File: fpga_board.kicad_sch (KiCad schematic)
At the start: 157 parts, among them Q1 2N7002PW, Q2 2N7002PW, Q3 2N7002PW, Q4 2N7002PW, Q5 2N7002PW, Q6 2N7002PW, SW1 1TS028A-1300-0600-CT, U1 LFE5U-45F-7BG256I, U10 TLV62569DRL, U2 CYUSB3014-BZXC, U3 TLV62569DRL, U5 K4B4G1646E-BCMA, U6 K4B4G1646E-BCMA, U7 TLV62569DRL, U8 TLV62569DRL, U9 TLV62569DRL, X1 XO32, Y1 Crystal_GND24

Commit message: fpga active oscillator pin changed and layout fully constructed. B.Cu ACC lines slightly modified and FPGA fifo lanes slightly modified to free GPLL input pin
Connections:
- net 1v35: now also C57.1, R24.1, X1.4 (V+)
- net 3v3: no longer C57.1, R24.1, X1.4 (V+)
- net FIFO_DQ21: now also U1.B4 (PT11B); no longer U1.C5 (PT15A)
- net FIFO_DQ25: now also U1.D5 (PT13B); no longer U1.B3 (PT4B)
- net FIFO_DQ28: now also U1.C5 (PT15A); no longer U1.B4 (PT11B)
- net FIFO_DQ30: now also U1.B3 (PT4B); no longer U1.A2 (PT4A)
- net FPGA_CLK: now also U1.A2 (PT4A); no longer U1.T6 (PB4A)
- no-connect marks 75 -> 74
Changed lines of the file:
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@@
 	)
 	(no_connect
-		(at 370.84 557.53)
-	)
-	(no_connect
 		(at 148.59 542.29)
 	)
@@
 	)
 	(bus_entry
+		(at 387.35 557.53)
+		(size 2.54 -2.54)
+		(stroke
+			(width 0)
+			(type default)
+		)
+	)
+	(bus_entry
 		(at 386.08 458.47)
 		(size -2.54 2.54)
@@
 	)
 	(bus_entry
-		(at 389.89 544.83)
-		(size -2.54 2.54)
-		(stroke
-			(width 0)
-			(type default)
-		)
-	)
-	(bus_entry
 		(at 662.94 68.58)
 		(size 2.54 2.54)
@@
 	)
 	(bus_entry
-		(at 299.72 542.29)
-		(size 2.54 2.54)
-		(stroke
-			(width 0)
-			(type default)
-		)
-	)
-	(bus_entry
 		(at 125.73 501.65)
 		(size 2.54 2.54)
@@
 	)
 	(bus_entry
+		(at 387.35 547.37)
+		(size 2.54 -2.54)
+		(stroke
+			(width 0)
+			(type default)
+		)
+	)
+	(bus_entry
 		(at 353.06 218.44)
 		(size -2.54 2.54)
@@
 	(wire
 		(pts
-			(xy 302.26 544.83) (xy 325.12 544.83)
-		)
-		(stroke
-			(width 0)
-			(type default)
-		)
-	)
-	(wire
-		(pts
 			(xy 450.85 238.76) (xy 450.85 241.3)
 		)
@@
 	(wire
 		(pts
-			(xy 370.84 547.37) (xy 387.35 547.37)
-		)
-		(stroke
-			(width 0)
-			(type default)
-		)
-	)
-	(wire
-		(pts
 			(xy 784.86 114.3) (xy 774.7 114.3)
 		)
@@
 		)
 	)
+	(bus
+		(pts
+			(xy 389.89 544.83) (xy 389.89 547.37)
+		)
+		(stroke
+			(width 0)
+			(type default)
+		)
+	)
 	(wire
 		(pts
@@
 	(bus
 		(pts
-			(xy 389.89 539.75) (xy 389.89 544.83)
-		)
-		(stroke
-			(width 0)
-			(type default)
-		)
-	)
-	(bus
-		(pts
 			(xy 125.73 501.65) (xy 125.73 504.19)
 		)
@@
 	(bus
 		(pts
-			(xy 299.72 530.86) (xy 299.72 542.29)
+			(xy 299.72 530.86) (xy 299.72 544.83)
 		)
 		(stroke
@@
 	(bus
 		(pts
-			(xy 389.89 544.83) (xy 389.89 547.37)
+			(xy 389.89 539.75) (xy 389.89 544.83)
 		)
 		(stroke
@@
 	(wire
 		(pts
+			(xy 370.84 547.37) (xy 387.35 547.37)
+		)
+		(stroke
+			(width 0)
+			(type default)
+		)
+	)
+	(wire
+		(pts
 			(xy 547.37 237.49) (xy 549.91 237.49)
 		)
@@
 	(wire
 		(pts
+			(xy 370.84 557.53) (xy 387.35 557.53)
+		)
+		(stroke
+			(width 0)
+			(type default)
+		)
+	)
+	(wire
+		(pts
 			(xy 664.21 142.24) (xy 678.18 142.24)
 		)
@@
 		)
 	)
-	(bus
-		(pts
-			(xy 299.72 542.29) (xy 299.72 544.83)
-		)
-		(stroke
-			(width 0)
-			(type default)
-		)
-	)
 	(label "DM0"
 		(at 279.4 138.43 0)
@@
 		)
 	)
-	(label "FIFO_DQ28"
+	(label "FIFO_DQ21"
 		(at 370.84 549.91 0)
 		(effects
@@
 		)
 	)
-	(label "FIFO_DQ30"
-		(at 311.15 544.83 0)
+	(label "FIFO_DQ31"
+		(at 370.84 547.37 0)
 		(effects
 			(font
@@
 		)
 	)
-	(label "FIFO_DQ25"
+	(label "FIFO_DQ30"
 		(at 311.15 547.37 0)
 		(effects
@@
 		)
 	)
-	(label "FIFO_DQ21"
+	(label "FIFO_DQ28"
 		(at 571.5 463.55 0)
 		(effects
@@
 		)
 	)
-	(label "FIFO_DQ31"
-		(at 370.84 547.37 0)
+	(label "FIFO_DQ25"
+		(at 370.84 557.53 0)
 		(effects
 			(font
@@
 		)
 	)
-	(global_label "3v3"
+	(global_label "1v35"
 		(shape input)
 		(at 170.18 384.81 180)
@@
 		)
 		(property "Intersheetrefs" "${INTERSHEET_REFS}"
-			(at 163.8082 384.81 0)
+			(at 162.5987 384.81 0)
 			(effects
 				(font
@@
 	(global_label "FPGA_CLK"
 		(shape input)
-		(at 148.59 466.09 180)
+		(at 325.12 544.83 180)
 		(fields_autoplaced yes)
 		(effects
@@
 		)
 		(property "Intersheetrefs" "${INTERSHEET_REFS}"
-			(at 136.3519 466.09 0)
+			(at 312.8819 544.83 0)
 			(effects
 				(font

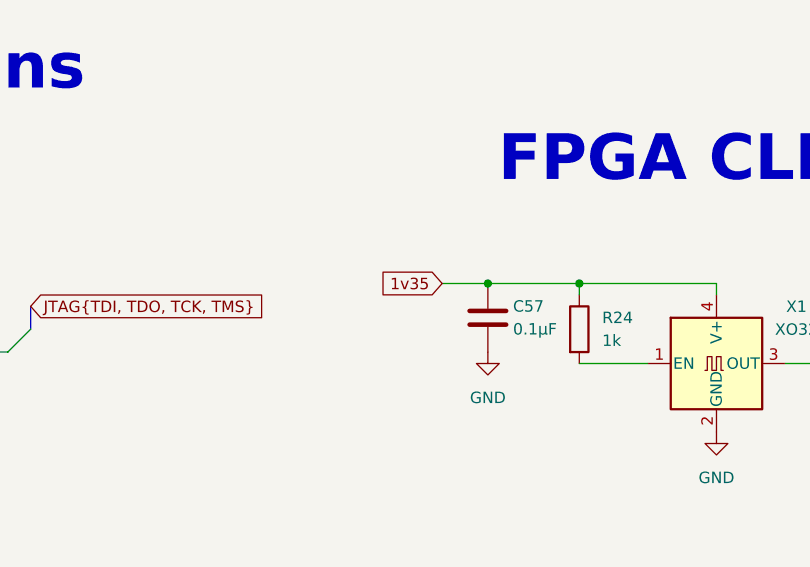
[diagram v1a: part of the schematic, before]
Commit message: oscillator core voltage fixed. changed from 1v35 to 3v3.
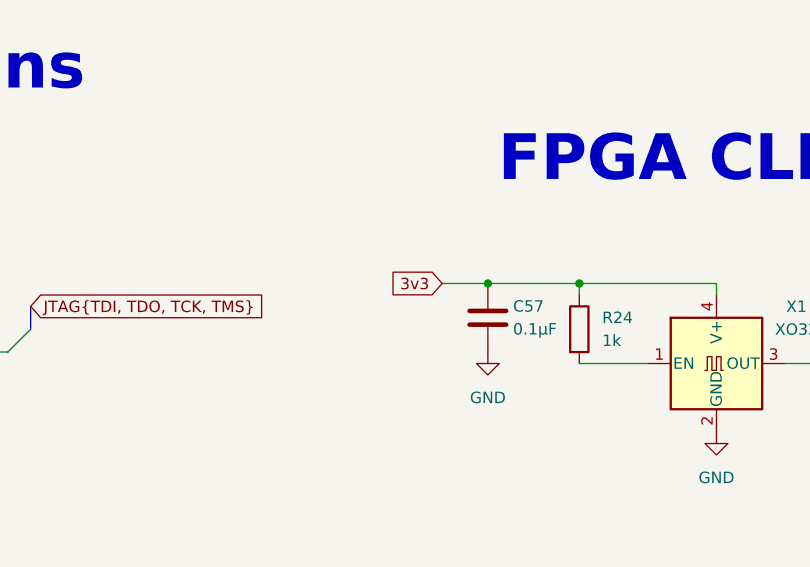
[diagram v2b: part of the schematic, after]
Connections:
- net 1v35: no longer C57.1, R24.1, X1.4 (V+)
- net 3v3: now also C57.1, R24.1, X1.4 (V+)
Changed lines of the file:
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@@
 		)
 	)
-	(global_label "1v35"
+	(global_label "3v3"
 		(shape input)
 		(at 170.18 384.81 180)
@@
 		)
 		(property "Intersheetrefs" "${INTERSHEET_REFS}"
-			(at 162.5987 384.81 0)
+			(at 163.8082 384.81 0)
 			(effects
 				(font

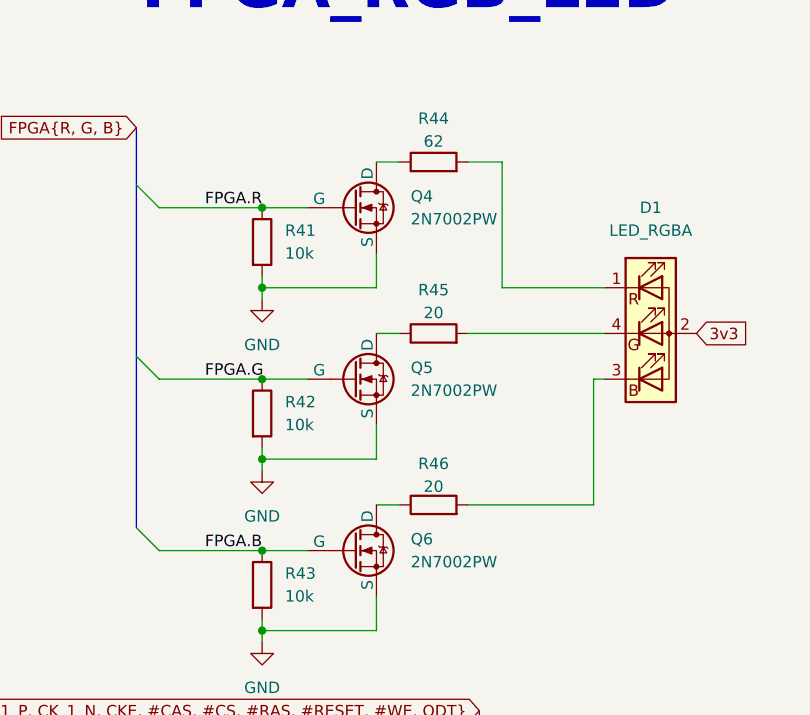
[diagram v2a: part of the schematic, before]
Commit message: added FX3 RGB in layout. wired 1v2 FX3 core. wired DONE pullup.
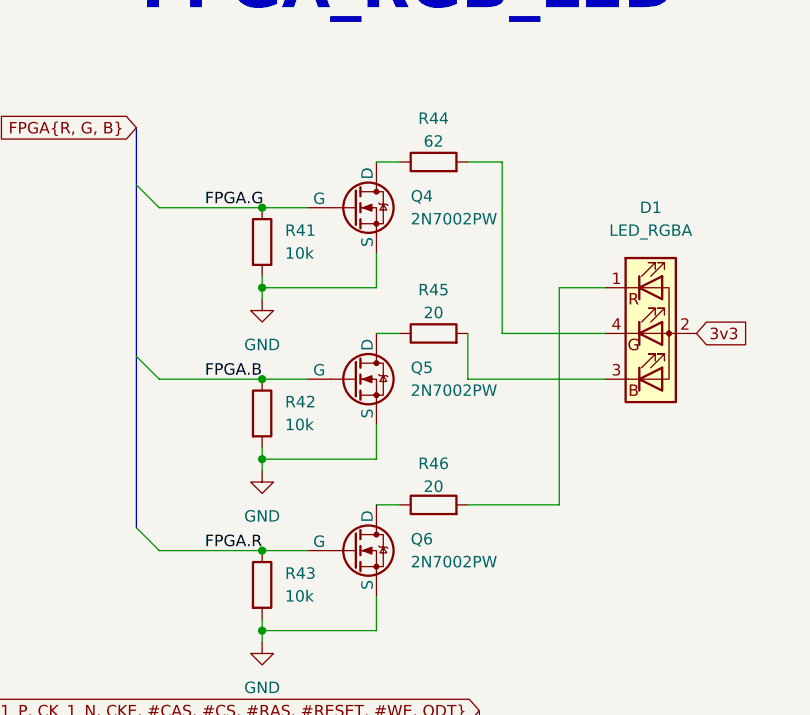
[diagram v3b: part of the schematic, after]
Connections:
- net FPGA.B: now also Q5.2 (G), R42.1; no longer Q6.2 (G), R43.1
- net FPGA.G: now also Q4.2 (G), R41.1; no longer Q5.2 (G), R42.1
- net FPGA.R: now also Q6.2 (G), R43.1; no longer Q4.2 (G), R41.1
- net at R45.2: now also D1.3 (BK); no longer D1.4 (GK)
- net at R44.2: now also D1.4 (GK); no longer D1.1 (RK)
- net at R46.2: now also D1.1 (RK); no longer D1.3 (BK)
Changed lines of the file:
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@@
 		)
 	)
+	(wire
+		(pts
+			(xy 320.04 368.3) (xy 325.12 368.3)
+		)
+		(stroke
+			(width 0)
+			(type default)
+		)
+	)
 	(bus
 		(pts
@@
 	(wire
 		(pts
-			(xy 325.12 368.3) (xy 313.69 368.3)
-		)
-		(stroke
-			(width 0)
-			(type default)
-		)
-	)
-	(wire
-		(pts
 			(xy 781.05 410.21) (xy 781.05 412.75)
 		)
@@
 	(wire
 		(pts
-			(xy 323.85 392.43) (xy 309.88 392.43)
-		)
-		(stroke
-			(width 0)
-			(type default)
-		)
-	)
-	(wire
-		(pts
 			(xy 266.7 107.95) (xy 284.48 107.95)
 		)
@@
 	(wire
 		(pts
+			(xy 313.69 373.38) (xy 325.12 373.38)
+		)
+		(stroke
+			(width 0)
+			(type default)
+		)
+	)
+	(wire
+		(pts
 			(xy 302.26 547.37) (xy 325.12 547.37)
 		)
@@
 		)
 	)
-	(wire
-		(pts
-			(xy 309.88 373.38) (xy 325.12 373.38)
-		)
-		(stroke
-			(width 0)
-			(type default)
-		)
-	)
 	(bus
 		(pts
@@
 	(wire
 		(pts
-			(xy 323.85 378.46) (xy 323.85 392.43)
-		)
-		(stroke
-			(width 0)
-			(type default)
-		)
-	)
-	(wire
-		(pts
 			(xy 781.05 427.99) (xy 781.05 430.53)
 		)
@@
 	(wire
 		(pts
+			(xy 309.88 378.46) (xy 325.12 378.46)
+		)
+		(stroke
+			(width 0)
+			(type default)
+		)
+	)
+	(wire
+		(pts
 			(xy 781.05 514.35) (xy 781.05 516.89)
 		)
@@
 		)
 	)
-	(wire
-		(pts
-			(xy 325.12 378.46) (xy 323.85 378.46)
-		)
-		(stroke
-			(width 0)
-			(type default)
-		)
-	)
 	(bus
 		(pts
@@
 		)
 	)
+	(wire
+		(pts
+			(xy 320.04 392.43) (xy 320.04 368.3)
+		)
+		(stroke
+			(width 0)
+			(type default)
+		)
+	)
 	(bus
 		(pts
@@
 		)
 	)
+	(wire
+		(pts
+			(xy 309.88 373.38) (xy 309.88 378.46)
+		)
+		(stroke
+			(width 0)
+			(type default)
+		)
+	)
 	(bus
 		(pts
@@
 	(wire
 		(pts
-			(xy 313.69 368.3) (xy 313.69 354.33)
+			(xy 313.69 354.33) (xy 313.69 373.38)
 		)
 		(stroke
@@
 		)
 	)
+	(wire
+		(pts
+			(xy 309.88 392.43) (xy 320.04 392.43)
+		)
+		(stroke
+			(width 0)
+			(type default)
+		)
+	)
 	(bus
 		(pts
@@
 		)
 	)
-	(label "FPGA.G"
+	(label "FPGA.B"
 		(at 280.67 378.46 0)
 		(effects
@@
 		)
 	)
-	(label "FPGA.B"
+	(label "FPGA.R"
 		(at 280.67 397.51 0)
 		(effects
@@
 		)
 	)
-	(label "FPGA.R"
+	(label "FPGA.G"
 		(at 280.67 359.41 0)
 		(effects

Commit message: updated DDR3 footprint BGA diameter from 0.4mm to 0.45mm for better stability I guess?
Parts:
- U5, U6: footprint Package_BGA:Micron_FBGA-96_7.5x13.5mm_Layout9x16_P0.8mm -> Package_BGA:Micron_FBGA-96_9x14mm_Layout9x16_P0.8mm
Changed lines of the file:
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@@
 			)
 		)
-		(property "Footprint" "Package_BGA:Micron_FBGA-96_7.5x13.5mm_Layout9x16_P0.8mm"
+		(property "Footprint" "Package_BGA:Micron_FBGA-96_9x14mm_Layout9x16_P0.8mm"
 			(at 450.85 231.14 0)
 			(effects
@@
 			)
 		)
-		(property "Footprint" "Package_BGA:Micron_FBGA-96_7.5x13.5mm_Layout9x16_P0.8mm"
+		(property "Footprint" "Package_BGA:Micron_FBGA-96_9x14mm_Layout9x16_P0.8mm"
 			(at 406.4 210.82 0)
 			(effects
@@
 			)
 		)
-		(property "Footprint" "Package_BGA:Micron_FBGA-96_7.5x13.5mm_Layout9x16_P0.8mm"
+		(property "Footprint" "Package_BGA:Micron_FBGA-96_9x14mm_Layout9x16_P0.8mm"
 			(at 450.85 92.71 0)
 			(effects
@@
 			)
 		)
-		(property "Footprint" "Package_BGA:Micron_FBGA-96_7.5x13.5mm_Layout9x16_P0.8mm"
+		(property "Footprint" "Package_BGA:Micron_FBGA-96_9x14mm_Layout9x16_P0.8mm"
 			(at 406.4 72.39 0)
 			(effects
@@
 			)
 		)
-		(property "Footprint" "Package_BGA:Micron_FBGA-96_7.5x13.5mm_Layout9x16_P0.8mm"
+		(property "Footprint" "Package_BGA:Micron_FBGA-96_9x14mm_Layout9x16_P0.8mm"
 			(at 284.48 62.23 0)
 			(effects
@@
 			)
 		)
-		(property "Footprint" "Package_BGA:Micron_FBGA-96_7.5x13.5mm_Layout9x16_P0.8mm"
+		(property "Footprint" "Package_BGA:Micron_FBGA-96_9x14mm_Layout9x16_P0.8mm"
 			(at 284.48 200.66 0)
 			(effects

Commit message: added correct decoupling in schematic for FPGA, currently working on layout.
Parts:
- added C67, C68, C69, C70, C71, C72, C77, C78, C79, C81, C83, C84, C85: 0.1µF, Capacitor_SMD:C_0402_1005Metric, symbol Device:C
- added C73, C74, C75, C76, C86: 10µF, Capacitor_SMD:C_0402_1005Metric, symbol Device:C
- added C80, C82: 22µF, Capacitor_SMD:C_0603_1608Metric, symbol Device:C
- added FB1: 120, Inductor_SMD:L_0603_1608Metric, symbol Device:FerriteBead
- C53, C54, C55: value 4.7µF -> 22µF; footprint Capacitor_SMD:C_0402_1005Metric -> Capacitor_SMD:C_0603_1608Metric
- C66: value 0.1µF -> 22µF; footprint Capacitor_SMD:C_0402_1005Metric -> Capacitor_SMD:C_0603_1608Metric
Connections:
- net 1v1: now also C67.2, C68.2, C69.2, C70.2, C71.2, C72.2, C73.1, C74.1, C75.1
- net 1v35: now also C65.2, C66.1
- net 2v5: now also FB1.1; no longer C65.2, C66.2
- net 3v3: now also C79.2, C80.1, C81.2, C82.1, C83.2, C84.2, C85.2, C86.1
- net GND: now also C66.2, U1.L5 (PL38D), C67.1, C68.1, C69.1, C70.1, C71.1, C72.1, C73.2, C74.2, C75.2, C76.2, C77.1, C78.1, C79.1, C80.2, C81.1, C82.2, C83.1, C84.1, C85.1, C86.2; no longer C66.1
- new net: C76.1, C77.2, C78.2, FB1.2
- no-connect marks 74 -> 73
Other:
- note added: "Bank 0 and 1"
- note added: "Bank 2,3,6 and 7"
- note added: "Bank 8"
- note added: "VCC"
- note added: "VCCAUX"
- note added: "grounded unused pin for easier decoupling"
- note removed: "Deal with decoupling capacitors later idk lol"
- note removed: "Vcc_1v1"
- moved on the sheet: C46, C47, C48, C49, C50, C51, C52, C53

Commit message: FPGA decoupling capacitors finished
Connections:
- net 2v5: no longer U1.G11 (VCCAUX), U1.L7 (VCCAUX)
- net GND: no longer U1.L5 (PL38D)
- net VCCAUX: now reaches C76.1, C77.2, C78.2, FB1.2
- net VCCAUX: now also U1.G11 (VCCAUX), U1.L7 (VCCAUX)
- no-connect marks 73 -> 74
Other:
- note removed: "grounded unused pin for easier decoupling"
- moved on the sheet: C67, C68, C69, C70, C71, C72, C73, C74, C75, C76, C77, C78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

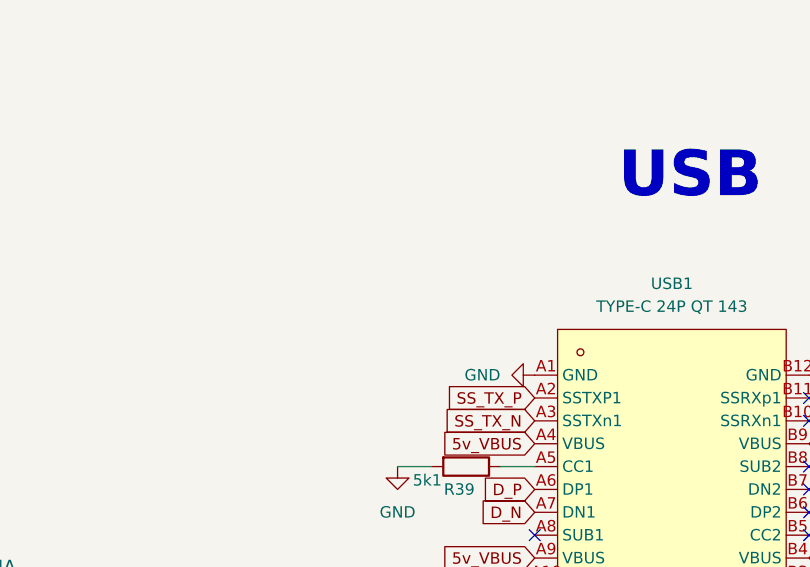
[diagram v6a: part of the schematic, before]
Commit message: rearanged RGB LEDs, added 3D models for most components, Added Electrolytic capacitors for VBUS, changed position of JTAG pins and other minor details
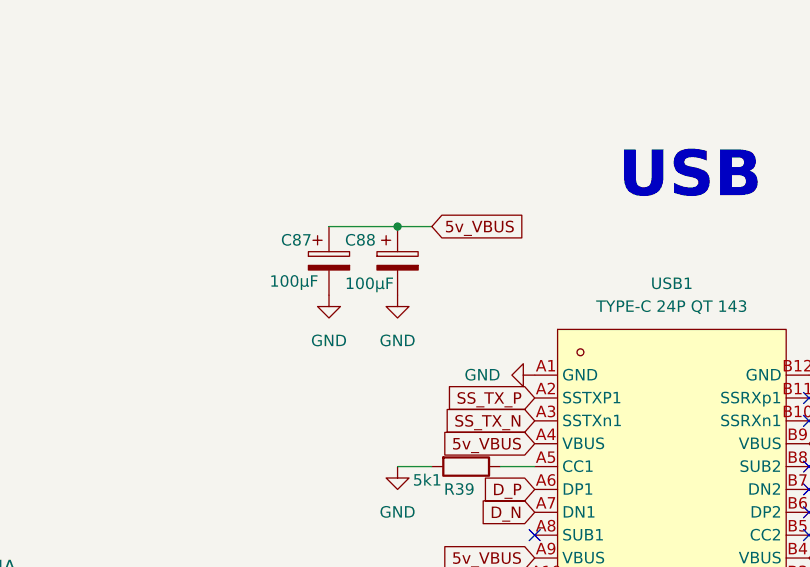
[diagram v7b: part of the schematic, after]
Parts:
- added C87, C88: 100μF, Capacitor_SMD:CP_Elec_6.3x5.4, symbol Device:C_Polarized
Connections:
- net 5v_VBUS: now also C87.1, C88.1
- net GND: now also C87.2, C88.2
